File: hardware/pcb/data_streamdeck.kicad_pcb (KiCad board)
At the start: 2 copper layers, 55 x 112 mm, 49 parts, among them J1 ScreenKey 1, J2 ScreenKey 2, J3 ScreenKey 3, J4 ScreenKey 4, J5 ScreenKey 5, J6 ScreenKey 6, J7 USB4105-GF-A, J8 microSD, SW1 BOOT, SW2 RESET, U1 ESP32-S3-WROOM-1-N16R8, U2 AMS1117-3.3, U3 USBLC6-2SC6

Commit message: Companion app v0.2: dynamic pages, live tiles, plugin store, in-app firmware updater
- Firmware v0.11: user-resizable pages (SET_PAGES 1-8, NVS-persisted), 48 key
  slots, page-switch HID codes 230-239, SET_FACE draw-only frames for tiles
- Companion: Tauri desktop app with page tabs (+/- to add/remove), live tiles
  (clock/timer/CPU/volume/now-playing/OBS), drag-to-swap keys, copy/paste,
  undo/redo, onboarding wizard with starter profiles
- Plugin store: registry-driven install/update/uninstall, hot reload, scaffold
  tool; reference plugins (Home Assistant webhook, Pomodoro)
- In-app firmware updater (espflash) with bootloader recovery (download-latch
  clear + RTC watchdog reset); bootloader ports excluded from auto-connect
- Profiles v4 carry page count, actions, and media; shareable .osdprofile.json
- Test backbone: 48 Playwright e2e + 38 unit + Rust tests, CI workflow
  (web/rust/firmware), signed auto-update via tauri-plugin-updater
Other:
- board text added: "OPEN SCREEN DECK"
- board text added: "OPEN SCREEN DECK · REV B"
- board text added: "REV B · 2026"
- board text added: "vcazan.github.io/open-screen-deck"

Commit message: Hardware Rev C: microSD was flipped inward — fix connector and case slot
Two build-verified problems from the first assembled unit:

- PCB: J8 (Hirose DM3D-SF) was rotated so the card inserted from the
  middle of the board. Rotated 180 deg (rot -90 -> 90) so the mouth faces
  the x=55 edge, re-routed SD_CS/MOSI/SCK/MISO/+3V3 to the mirrored pads,
  detoured KEY6 around a relocated shield pad, and re-stitched GND. DRC
  back to the Rev B baseline (0 new violations, 0 unconnected). Silk and
  gerbers regenerated as REV C.
- Enclosure v12: the SD slot was cut in the wrong side wall — KiCad's
  top view mirrors x when the board sits component-up, which v11 missed.
  Slot moved to the wall adjacent to the kicad x=55 edge (deck right as
  you face it), corner screw axes corrected for the same mirror (0.1 mm),
  STLs re-exported as v12.

Docs updated (PCB placements, mechanical contract, parts list, assembly).
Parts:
- turned J8 to 90 degrees
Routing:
- net MISO: track 34.5 -> 53.0 mm
- net SCK: track 218.7 -> 235.0 mm, vias 9 -> 10
- net +3V3: track 289.8 -> 298.6 mm, vias 4 -> 7
- net SD_CS: track 39.3 -> 48.1 mm
- net MOSI: track 251.5 -> 255.9 mm, vias 11 -> 12
- net GND: track 36.8 -> 33.2 mm, vias 50 -> 47
- net KEY6: track 71.1 -> 71.7 mm, vias 4 -> 6
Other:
- board text added: "OPEN SCREEN DECK · REV C"
- board text added: "REV C · 2026"
- board text removed: "OPEN SCREEN DECK · REV B"
- board text removed: "REV B · 2026"

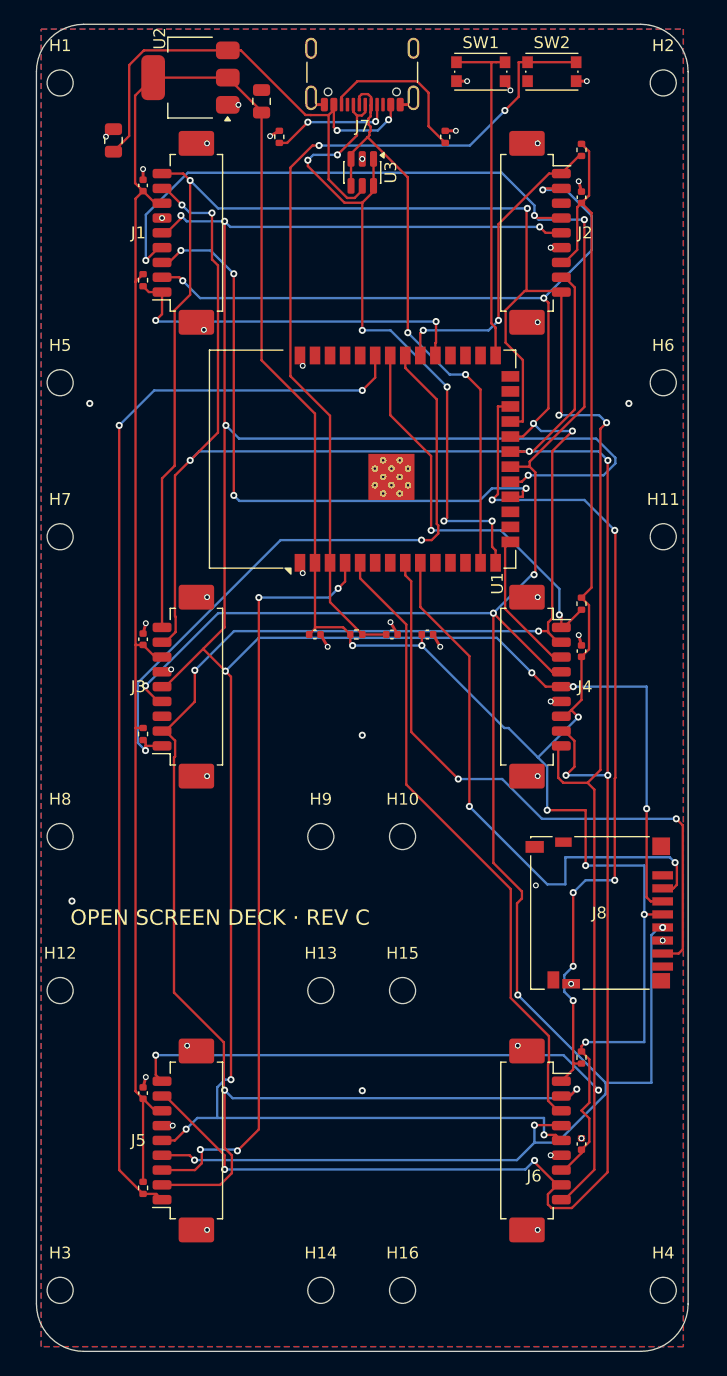
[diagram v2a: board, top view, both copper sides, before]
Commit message: Rev C: reroute J8 with freerouting instead of hand-drawn edge channels
The hand-routed approaches ran two traces 0.25 mm from the board edge.
Ripped them out and let freerouting route SD_CS/MOSI/SCK/MISO/+3V3 to
the rotated connector — everything now stays >= 1.3 mm from the edge
(the closest copper is the connector's own pads). Restored the via
drills the SES import inflated, cleaned up freerouting's one dangling
stub, DRC back to baseline (0 new violations, 0 unconnected). Gerbers
and the JLCPCB zip regenerated.
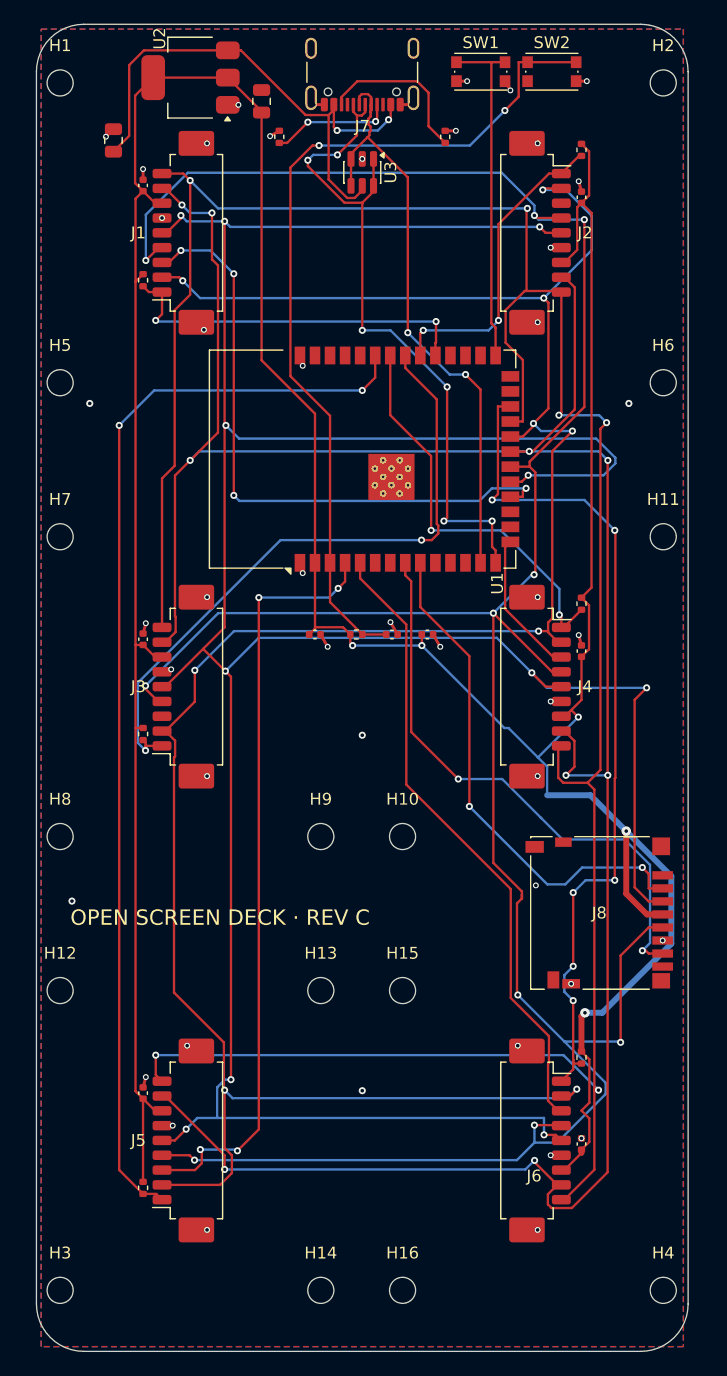
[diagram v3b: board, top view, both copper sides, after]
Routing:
- net +3V3: track 298.6 -> 303.5 mm, vias 7 -> 5
- net SD_CS: track 48.1 -> 43.3 mm
- net MISO: track 53.0 -> 48.6 mm
- net MOSI: track 255.9 -> 259.8 mm, vias 12 -> 11
- net SCK: track 235.0 -> 234.4 mm

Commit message: Hardware Rev D + enclosure v13: real module dimensions from vendor CAD
The marketing outline drawing labels the KEYCAP (21.89 x 25.13, which
rounds to the 22.0/25.3 we misread as the hole pattern). Waveshare now
publishes official CAD (STEP/DXF/PDF, 2026-07-10) with the truth:
mounting holes 20.0 x 29.25, keycap 21.89 x 25.13 rectangular, factory
standoffs 8.0 mm, module PCB 26.01 x 35.31, cap-to-rear-PCB 16.0.

- PCB Rev D: all 16 mounting holes (12 standoff + 4 corner case screws)
  moved to the real pattern; skip positions re-derived (ESP32 / USB /
  microSD conflicts); one GND stitch via relocated; DRC clean.
- Enclosure v13: rectangular keycap apertures (+0.6 clearance), hole
  pattern + corner screw axes updated, stack redone for 8.0 mm
  standoffs (module body 7.4 -> face height unchanged), corner spacers
  now 8.0 mm. STLs re-exported; aperture and insert geometry verified
  from the meshes.
- ScreenKey replica model rebuilt to the vendor drawing; official
  STEP/PDF checked into docs/reference with a warning about the
  marketing-drawing trap. Docs updated throughout.

Bottom, top, and spacers need re-printing; the stand is unchanged.
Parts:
- moved H10 2.21 mm to (31.9, 70.5)
- moved H14 2.21 mm to (23.0, 108.8)
- moved H16 2.21 mm to (31.9, 108.8)
- moved H3 2.21 mm to (3.00, 108.8)
- moved H4 2.21 mm to (51.9, 108.8)
- moved H8 2.21 mm to (3.00, 70.5)
- moved H9 2.21 mm to (23.0, 70.5)
- moved H11 2.21 mm to (51.9, 41.3)
- moved H5 2.21 mm to (3.00, 32.2)
- moved H6 2.21 mm to (51.9, 32.2)
- moved H7 2.21 mm to (3.00, 41.3)
- moved H1 2.21 mm to (3.00, 2.98)
- moved H2 2.21 mm to (51.9, 2.98)
- moved H12 2.21 mm to (3.00, 79.6)
- moved H13 2.21 mm to (23.0, 79.6)
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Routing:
- net GND: vias 47 -> 46
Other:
- board text added: "OPEN SCREEN DECK · REV D"
- board text added: "REV D · 2026"
- board text removed: "OPEN SCREEN DECK · REV C"
- board text removed: "REV C · 2026"
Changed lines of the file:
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@@
 	(paper "A4")
 	(title_block
-		(rev "C")
+		(rev "D")
 	)
 	(layers
@@
 	(footprint "MountingHole:MountingHole_2.2mm_M2"
 		(layer "F.Cu")
-		(at 52.9 43.25)
+		(at 51.9 41.275)
 		(descr "Mounting Hole 2.2mm, M2, no annular, generated by kicad-footprint-generator mountinghole.py")
 		(tags "mountinghole M2")
@@
 			(at 0 -3.15 0)
 			(layer "F.SilkS")
+			(hide yes)
 			(effects
 				(font
@@
 	(footprint "MountingHole:MountingHole_2.2mm_M2"
 		(layer "F.Cu")
-		(at 30.9 68.55)
+		(at 31.9 70.525)
 		(descr "Mounting Hole 2.2mm, M2, no annular, generated by kicad-footprint-generator mountinghole.py")
 		(tags "mountinghole M2")
@@
 			(at 0 -3.15 0)
 			(layer "F.SilkS")
+			(hide yes)
 			(effects
 				(font
@@
 	(footprint "MountingHole:MountingHole_2.2mm_M2"
 		(layer "F.Cu")
-		(at 24 106.85)
+		(at 23 108.825)
 		(descr "Mounting Hole 2.2mm, M2, no annular, generated by kicad-footprint-generator mountinghole.py")
 		(tags "mountinghole M2")
@@
 			(at 0 -3.15 0)
 			(layer "F.SilkS")
+			(hide yes)
 			(effects
 				(font
@@
 	(footprint "MountingHole:MountingHole_2.2mm_M2"
 		(layer "F.Cu")
-		(at 52.9 106.85)
+		(at 51.9 108.825)
 		(descr "Mounting Hole 2.2mm, M2, no annular, generated by kicad-footprint-generator mountinghole.py")
 		(tags "mountinghole M2")
@@
 			(at 0 -3.15 0)
 			(layer "F.SilkS")
+			(hide yes)
 			(effects
 				(font
@@
 	(footprint "MountingHole:MountingHole_2.2mm_M2"
 		(layer "F.Cu")
-		(at 30.9 81.55)
+		(at 31.9 79.575)
 		(descr "Mounting Hole 2.2mm, M2, no annular, generated by kicad-footprint-generator mountinghole.py")
 		(tags "mountinghole M2")
@@
 			(at 0 -3.15 0)
 			(layer "F.SilkS")
+			(hide yes)
 			(effects
 				(font
@@
 	(footprint "MountingHole:MountingHole_2.2mm_M2"
 		(layer "F.Cu")
-		(at 2 68.55)
+		(at 3 70.525)
 		(descr "Mounting Hole 2.2mm, M2, no annular, generated by kicad-footprint-generator mountinghole.py")
 		(tags "mountinghole M2")
@@
 			(at 0 -3.15 0)
 			(layer "F.SilkS")
+			(hide yes)
 			(effects
 				(font
@@
 	(footprint "MountingHole:MountingHole_2.2mm_M2"
 		(layer "F.Cu")
-		(at 52.9 4.95)
+		(at 51.9 2.975)
 		(descr "Mounting Hole 2.2mm, M2, no annular, generated by kicad-footprint-generator mountinghole.py")
 		(tags "mountinghole M2")
@@
 			(at 0 -3.15 0)
 			(layer "F.SilkS")
+			(hide yes)
 			(effects
 				(font
@@
 	(footprint "MountingHole:MountingHole_2.2mm_M2"
 		(layer "F.Cu")
-		(at 2 4.95)
+		(at 3 2.975)
 		(descr "Mounting Hole 2.2mm, M2, no annular, generated by kicad-footprint-generator mountinghole.py")
 		(tags "mountinghole M2")
@@
 			(at 0 -3.15 0)
 			(layer "F.SilkS")
+			(hide yes)
 			(effects
 				(font
@@
 	(footprint "MountingHole:MountingHole_2.2mm_M2"
 		(layer "F.Cu")
-		(at 24 81.55)
+		(at 23 79.575)
 		(descr "Mounting Hole 2.2mm, M2, no annular, generated by kicad-footprint-generator mountinghole.py")
 		(tags "mountinghole M2")
@@
 			(at 0 -3.15 0)
 			(layer "F.SilkS")
+			(hide yes)
 			(effects
 				(font
@@
 	(footprint "MountingHole:MountingHole_2.2mm_M2"
 		(layer "F.Cu")
-		(at 2 30.25)
+		(at 3 32.225)
 		(descr "Mounting Hole 2.2mm, M2, no annular, generated by kicad-footprint-generator mountinghole.py")
 		(tags "mountinghole M2")
@@
 			(at 0 -3.15 0)
 			(layer "F.SilkS")
+			(hide yes)
 			(effects
 				(font
@@
 	(footprint "MountingHole:MountingHole_2.2mm_M2"
 		(layer "F.Cu")
-		(at 52.9 30.25)
+		(at 51.9 32.225)
 		(descr "Mounting Hole 2.2mm, M2, no annular, generated by kicad-footprint-generator mountinghole.py")
 		(tags "mountinghole M2")
@@
 			(at 0 -3.15 0)
 			(layer "F.SilkS")
+			(hide yes)
 			(effects
 				(font
@@
 	(footprint "MountingHole:MountingHole_2.2mm_M2"
 		(layer "F.Cu")
-		(at 24 68.55)
+		(at 23 70.525)
 		(descr "Mounting Hole 2.2mm, M2, no annular, generated by kicad-footprint-generator mountinghole.py")
 		(tags "mountinghole M2")
@@
 			(at 0 -3.15 0)
 			(layer "F.SilkS")
+			(hide yes)
 			(effects
 				(font
@@
 	(footprint "MountingHole:MountingHole_2.2mm_M2"
 		(layer "F.Cu")
-		(at 2 43.25)
+		(at 3 41.275)
 		(descr "Mounting Hole 2.2mm, M2, no annular, generated by kicad-footprint-generator mountinghole.py")
 		(tags "mountinghole M2")
@@
 			(at 0 -3.15 0)
 			(layer "F.SilkS")
+			(hide yes)
 			(effects
 				(font
@@
 	(footprint "MountingHole:MountingHole_2.2mm_M2"
 		(layer "F.Cu")
-		(at 2 81.55)
+		(at 3 79.575)
 		(descr "Mounting Hole 2.2mm, M2, no annular, generated by kicad-footprint-generator mountinghole.py")
 		(tags "mountinghole M2")
@@
 			(at 0 -3.15 0)
 			(layer "F.SilkS")
+			(hide yes)
 			(effects
 				(font
@@
 	(footprint "MountingHole:MountingHole_2.2mm_M2"
 		(layer "F.Cu")
-		(at 30.9 106.85)
+		(at 31.9 108.825)
 		(descr "Mounting Hole 2.2mm, M2, no annular, generated by kicad-footprint-generator mountinghole.py")
 		(tags "mountinghole M2")
@@
 			(at 0 -3.15 0)
 			(layer "F.SilkS")
+			(hide yes)
 			(effects
 				(font
@@
 	(footprint "MountingHole:MountingHole_2.2mm_M2"
 		(layer "F.Cu")
-		(at 2 106.85)
+		(at 3 108.825)
 		(descr "Mounting Hole 2.2mm, M2, no annular, generated by kicad-footprint-generator mountinghole.py")
 		(tags "mountinghole M2")
@@
 			(at 0 -3.15 0)
 			(layer "F.SilkS")
+			(hide yes)
 			(effects
 				(font
@@
 		(layer "Edge.Cuts")
 	)
-	(gr_text "OPEN SCREEN DECK · REV C"
+	(gr_text "OPEN SCREEN DECK · REV D"
 		(at 15.5 75.4 0)
 		(layer "F.SilkS")
@@
 		)
 	)
-	(gr_text "REV C  ·  2026"
+	(gr_text "REV D  ·  2026"
 		(at 27.5 102.4 0)
 		(layer "B.SilkS")
@@
 		(drill 0.3)
 		(layers "F.Cu" "B.Cu")
-		(net "GND")
-	)
-	(via
-		(at 4.5 32)
-		(size 0.6)
-		(drill 0.3)
-		(layers "F.Cu" "B.Cu")
